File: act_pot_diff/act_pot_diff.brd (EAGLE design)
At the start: 160 x 100 mm, 11 parts, among them J1 FFC-32, J2 REF_GND, J3 SENSORS, J4 I2C, J5 GND, J6 VDD, U1 MCP3424T-E/ST, U2 LM340MPX-5.0230

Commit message: finish module and diff module
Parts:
- added C10, C11, C12, C14, C15, C16, C17, C7, C9: 0.1uF, scono:0402-CAP
- added C13, C8: 0.1uF, scono:0603-CAP
- added C2, C3, C4: 100nF, scono:0402-CAP
- added C5, C6: 18pF, scono:0402-CAP
- added D1: (no value), scono:LED-0603
- added D2: RED, scono:LED-0603
- added J10: I2C, scono:1X02
- added J12: BURNIN, scono:BURNIN
- added J9: (no value), scono:1X08
- added R1, R4, R5: 10k, scono:R0402
- added SW1: BTN-PTS810, scono:BTN_PTS810
- added TP1: TEST_POINTTHRU, scono:TEST_POINT
- added U3, U4: MCP3424T-E/ST, scono:TSSOP14_MC
- added Y1: 16MHz, scono:XTAL500X320X130N
- C1: value (none) -> 100nF; device scono:0603-CAP -> scono:0402-CAP
- J1: value FFC-32 -> VCC; device scono:MOLEX_503480-3200 -> scono:1X02
- J2: value REF_GND -> GND
- J3: value SENSORS -> UART; device scono:1X04 -> scono:1X02
- J4: value I2C -> FTDI; device scono:1X02 -> scono:1X06_NO_SILK
- J5: value GND -> VCC
- J6: value VDD -> GND
- R2, R3: value 10k -> 500R; device scono:0603-RES -> scono:R0402
- U1: value MCP3424T-E/ST -> LM340MPX-5.0230; device scono:TSSOP14_MC -> scono:SOT230P700X180-4N
- U2: value LM340MPX-5.0230 -> ATMEGA328P-AUR; device scono:SOT230P700X180-4N -> scono:QFP80P900X900X120-32N
- moved J6 107.4 mm to (30.5, 46.0), turned to 135 degrees
- moved U2 99.9 mm to (16.2, 22.0), turned to 180 degrees
- moved J2 94.7 mm to (30.2, 22.0), turned to 270 degrees
- moved J4 89.4 mm to (10.0, 7.50)
- moved J3 83.1 mm to (17.5, 11.0), turned to 180 degrees
- moved J5 72.9 mm to (2.00, 46.0), turned to 45 degrees
- moved R2 66.0 mm to (21.2, 11.0), turned to 90 degrees
- moved R3 63.5 mm to (11.2, 11.0), turned to 270 degrees
- moved C1 56.8 mm to (8.25, 19.0)
- moved U1 51.4 mm to (6.75, 13.2), turned to 270 degrees
- moved J1 49.8 mm to (2.25, 22.0), turned to 270 degrees
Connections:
- net VIN renamed GPIO1
- removed net K: J1.18, J1.19, J1.20, J1.21, J1.22, J3.3, U1.11
- removed net NA: J1.11, J1.12, J1.13, J1.14, J1.15, J3.2, U1.3
- removed net NH4: J1.4, J1.5, J1.6, J1.7, J1.8, J3.1, U1.1
- removed net REF_ELEC: J1.25, J1.26, J1.27, J1.28, J1.29, J2.1, J3.4, U1.12, U1.2, U1.4
- new net ADC0: U2.23
- new net ADC1: U2.24
- new net ADC2: U2.25
- new net ADC3: U2.26
- new net AREF: U2.20
- new net CH1: C9.2, J9.1, U3.1
- new net CH2: C10.2, J9.2, U3.3
- new net CH3: C11.2, J9.3, U3.11
- new net CH4: C12.2, J9.4, U3.13
- new net CH5: C14.2, J9.5, U4.1
- new net CH6: C15.2, J9.6, U4.3
- new net CH7: C16.2, J9.7, U4.11
- new net CH8: C17.2, J9.8, U4.13
- new net CTS: J4.5
- new net GPIO0: R2.2, U2.32
- new net GPIO2: U2.2
- new net GPIO3: U2.9
- new net GPIO4: U2.10
- new net GPIO5: U2.11
- new net GPIO6: U2.12
- new net GPIO7: U2.13
- new net MISO: J12.MISO, U2.16
- new net MOSI: J12.MOSI, U2.15
- new net N$3: D1.A, R2.1
- new net N$4: D2.A, R3.2
- new net N$5: C7.2, J4.1
- new net RST: C7.1, J12.RST, R1.1, SW1.3, SW1.4, U2.29
- new net RX: J3.1, J4.3, U2.30
- new net SCK: J12.SCK, U2.17
- new net SS: U2.14
- new net TX: J3.2, J4.2, U2.31
- new net VCC: C1.2, J1.1, J1.2, J5.1, J5.2, U1.1
- new net XTAL1: C5.1, U2.7, Y1.2
- new net XTAL2: C6.1, U2.8, Y1.1
- net 5V: now also C13.2, C2.2, C3.2, C4.2, C8.2, J12.3.3V, J4.4, R1.2, R3.1, R4.2, R5.2, TP1.1, U1.3, U2.18, U2.4, U2.6, U3.6, U4.10, U4.6; no longer C1.2, J6.1, J6.2, R2.2, R3.2, U1.6, U2.3
- net GND: now also C10.1, C11.1, C12.1, C13.1, C14.1, C15.1, C16.1, C17.1, C2.1, C3.1, C4.1, C5.2, C6.2, C8.1, C9.1, D1.C, D2.C, J12.GND, J2.1, J4.6, J6.1, J6.2, SW1.1, SW1.2, U1.2, U1.4, U2.21, U2.3, U2.5, U3.10, U3.12, U3.14, U3.2, U3.4, U3.5, U3.9, U4.12, U4.14, U4.2, U4.4, U4.5, U4.9; no longer J5.1, J5.2, U1.10, U1.5, U1.9, U2.2, U2.4
- net SCL: now also J10.1, R5.1, U2.28, U3.8, U4.8; no longer J4.1, R3.1, U1.8
- net SDA: now also J10.2, R4.1, U2.27, U3.7, U4.7; no longer J4.2, R2.1, U1.7
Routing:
- net GND: track 0.00 -> 94.1 mm, vias 0 -> 17
- net SDA: track 0.00 -> 43.0 mm, vias 0 -> 3
- net SCL: track 0.00 -> 42.3 mm, vias 0 -> 3
- net VCC: track 0.00 -> 40.3 mm
- net MISO: track 0.00 -> 26.7 mm, vias 0 -> 1
- net SCK: track 0.00 -> 26.3 mm, vias 0 -> 1
- net RST: track 0.00 -> 26.2 mm, vias 0 -> 1
- net MOSI: track 0.00 -> 24.8 mm, vias 0 -> 1
- net CH2: track 0.00 -> 18.0 mm, vias 0 -> 2
- net CH1: track 0.00 -> 17.7 mm, vias 0 -> 2
- net CH5: track 0.00 -> 17.4 mm, vias 0 -> 2
- net CH8: track 0.00 -> 16.9 mm, vias 0 -> 2
- net N$5: track 0.00 -> 16.5 mm
- net CH3: track 0.00 -> 16.5 mm, vias 0 -> 2
- net TX: track 0.00 -> 16.5 mm, vias 0 -> 2
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- added copper zone on layer 1, net 5V
- added copper zone on layer 16, net GND
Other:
- board size 160 x 100 mm -> 32.5 x 50 mm
- board text added: "Ch1"
- board text added: "Ch2"
- board text added: "Ch3"
- board text added: "Ch4"
- board text added: "Ch5"
- board text added: "Ch6"
- board text added: "Ch7"
- board text added: "Ch8"
- board text added: "GND"
- board text added: "VCC"

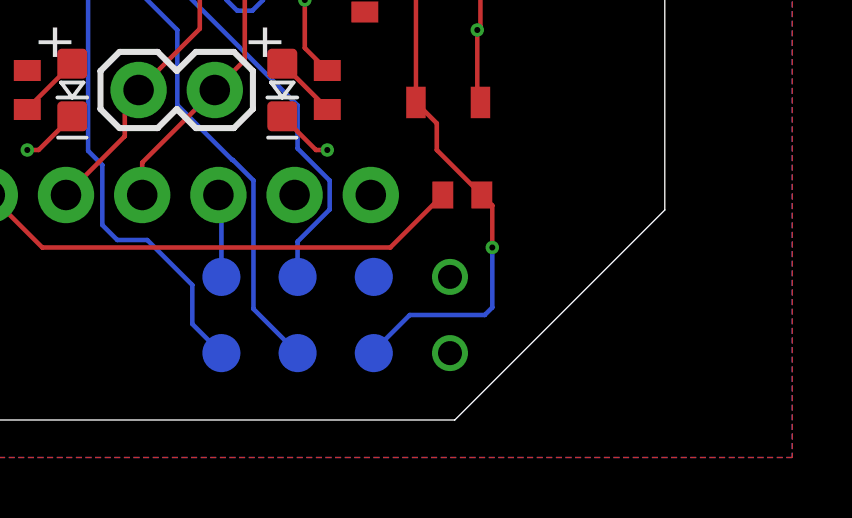
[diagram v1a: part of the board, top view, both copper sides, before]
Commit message: update burnin drill size
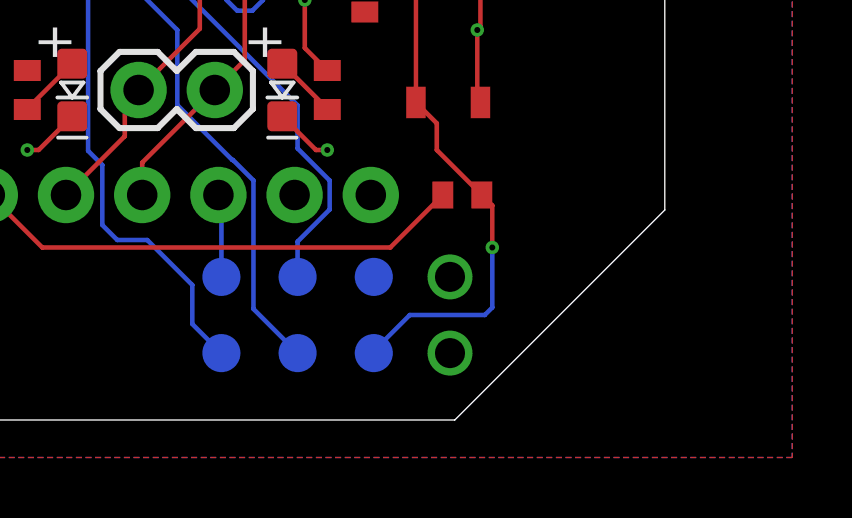
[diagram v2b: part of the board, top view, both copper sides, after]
